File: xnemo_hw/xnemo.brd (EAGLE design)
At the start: 39.7 x 29 mm, 20 parts, among them J1 MICRO_USB_B_RECEPT, J2 DM3D_MICRO_SD, U1 LTC3559, U2 L3GD20, U3 STM32F405RG, U5 HMC5883L, U6 ADXL345, X1 TXC_7A_XTAL

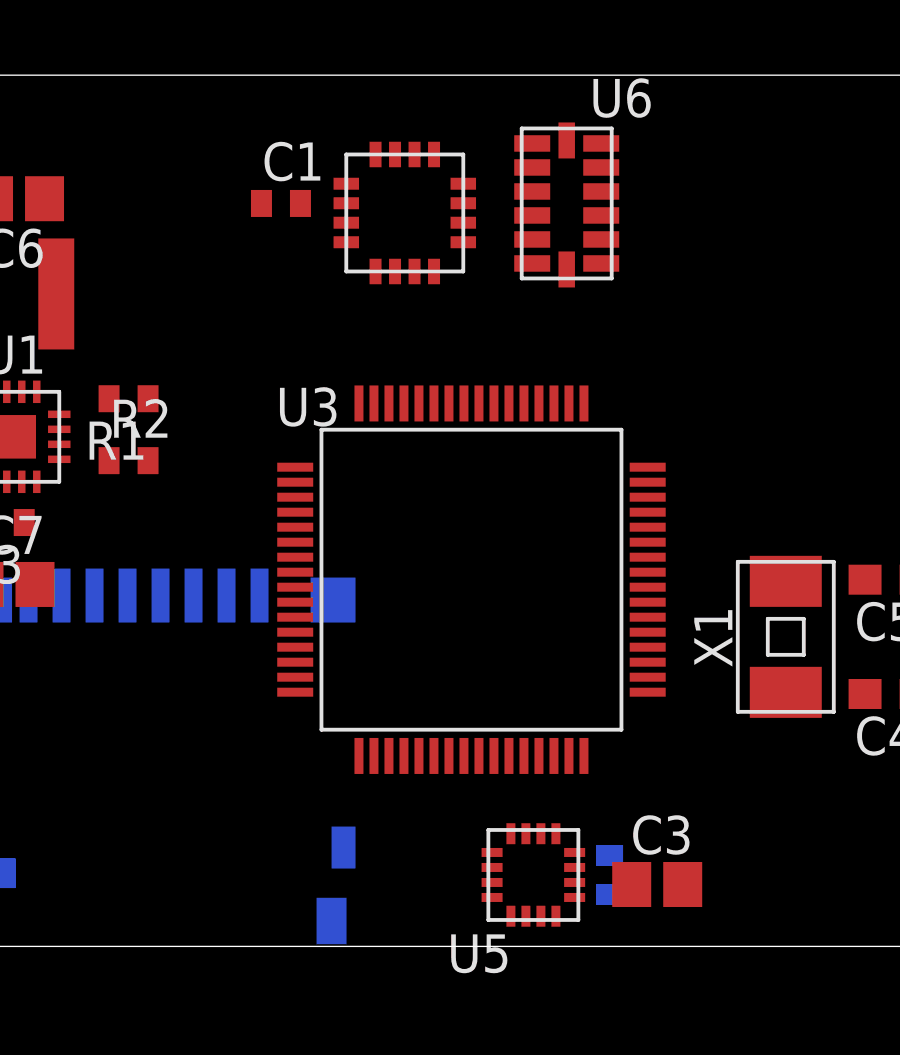
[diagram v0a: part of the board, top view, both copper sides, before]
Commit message: Updated some little things and added JTAG header
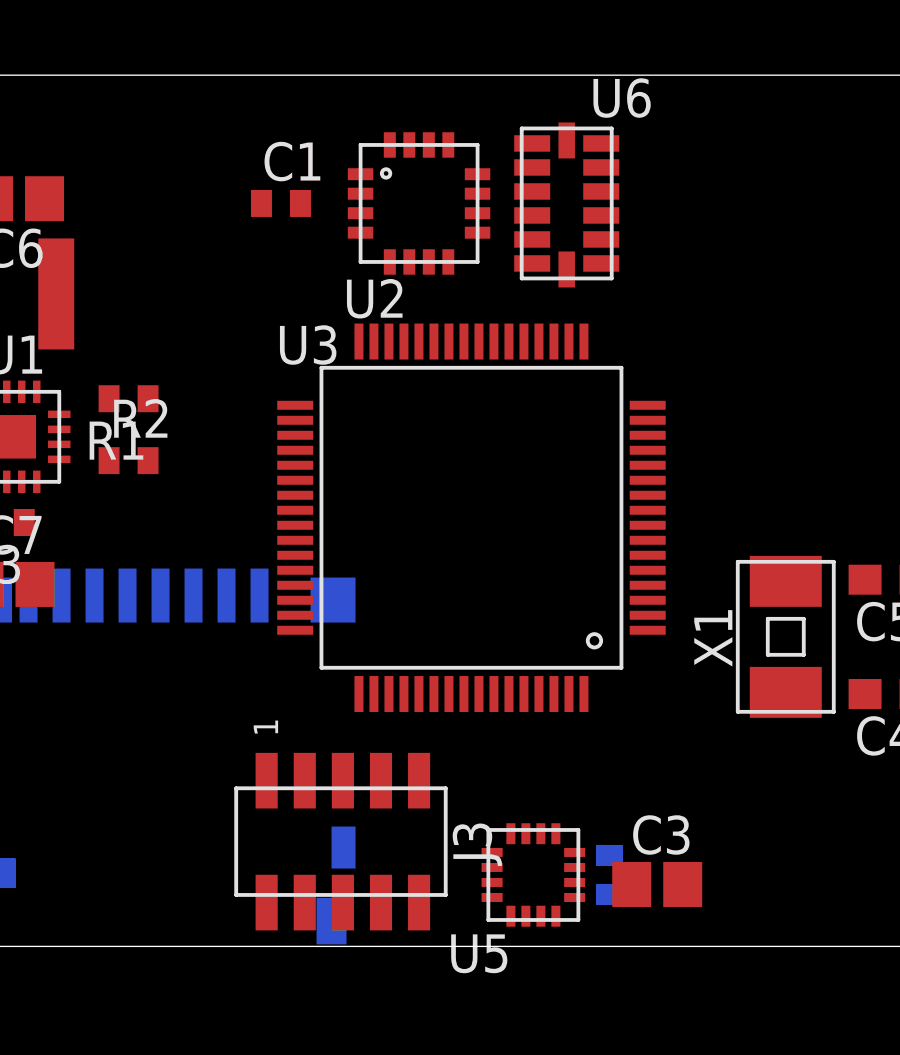
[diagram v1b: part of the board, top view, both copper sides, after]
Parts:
- added J3: HEADER_2X5, xnemo:HEADER_2X5_0.05_SMD
- moved U3 2.06 mm to (23.7, 14.3)
- moved U2 0.57 mm to (21.9, 24.8), turned to 0 degrees
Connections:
- net USB_HPWR renamed POW_HPWR
- net USB_SUSP renamed POW_SUSP
- new net JNTRST: U3.P$56
- new net JTCK: J3.4, U3.P$49
- new net JTDI: J3.8, U3.P$50
- new net JTDO: J3.6, U3.P$55
- new net JTMS: J3.2, U3.P$46
- new net POW_CHRG: U1.P$15
- new net RESET: J3.10, U3.P$7
- net 3V3: now also J3.1
- net GND: now also J3.3, J3.5, J3.7, J3.9

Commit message: Started bord
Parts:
- added C10, C11, C12, C9: 2.2u, resistor:C0603
- C4, C5: device resistor:C0603 -> resistor:C0402
- moved J3 10.5 mm to (8.89, 3.49)
- moved U2 8.04 mm to (14.0, 23.5), turned to 180 degrees
- moved U5 6.35 mm to (19.4, 2.54)
- moved C3 5.41 mm to (24.4, 2.38)
- moved U6 5.08 mm to (21.7, 24.9), turned to 270 degrees
- moved C4 4.98 mm to (32.7, 9.21), turned to 270 degrees
- moved C5 4.92 mm to (32.7, 12.4), turned to 90 degrees
- moved X1 4.00 mm to (30.2, 10.8)
- moved C1 3.74 mm to (13.7, 24.0), flipped to the bottom, turned to 270 degrees
- moved U3 3.17 mm to (21.1, 12.4)
- moved U1 2.43 mm to (6.03, 17.5)
- moved C2 2.23 mm to (26.0, 2.54)
- moved R2 2.01 mm to (10.3, 16.8), turned to 180 degrees
- moved R1 1.91 mm to (10.3, 18.3), turned to 0 degrees
- moved C8 0.79 mm to (4.13, 20.6), turned to 0 degrees
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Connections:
- net N$5 renamed GYR_RES
- removed net VBUS: C7.2, U1.P$16
- new net N$17: C10.1, U3.P$31
- new net N$5: C11.1, U3.P$47
- net 3V3: now also C12.1, C9.2
- net ACC_INT1: now also U3.P$27
- net ACC_INT2: now also U3.P$26
- net GND: now also C10.2, C11.2, C12.2, C9.1
- net GYR_DRDY: now also U3.P$34
- net GYR_INT1: now also U3.P$33
- net POW_CHRG: now also U3.P$28
- net POW_HPWR: now also U3.P$30
- net POW_SUSP: now also U3.P$29
- net SPI_CS_ACC: now also U3.P$25
- net SPI_CS_GYR: now also U3.P$35
- net VUSB: now also C7.2, U1.P$16
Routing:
- net 3V3: track 0.00 -> 30.6 mm
- net RESET: track 0.00 -> 23.5 mm, vias 0 -> 2
- net GYR_DRDY: track 0.00 -> 18.9 mm, vias 0 -> 2
- net SPI_CLK: track 0.00 -> 18.7 mm, vias 0 -> 2
- net GYR_INT1: track 0.00 -> 14.7 mm, vias 0 -> 2
- net JTDO: track 0.00 -> 14.6 mm
- net JTMS: track 0.00 -> 14.6 mm
- net JTCK: track 0.00 -> 12.5 mm
- net USB_D-: track 0.00 -> 11.0 mm
- net USB_D+: track 0.00 -> 11.0 mm
- net JTDI: track 0.00 -> 10.7 mm, vias 0 -> 2
- net SD_DAT3: track 0.00 -> 10.2 mm, vias 0 -> 1
- net SPI_MISO: track 0.00 -> 8.53 mm, vias 0 -> 1
- net SPI_MOSI: track 0.00 -> 8.01 mm, vias 0 -> 2
- net OSC_IN: track 0.00 -> 6.57 mm
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- added copper zone on layer 1, net GND
- added copper zone on layer 16, net GND

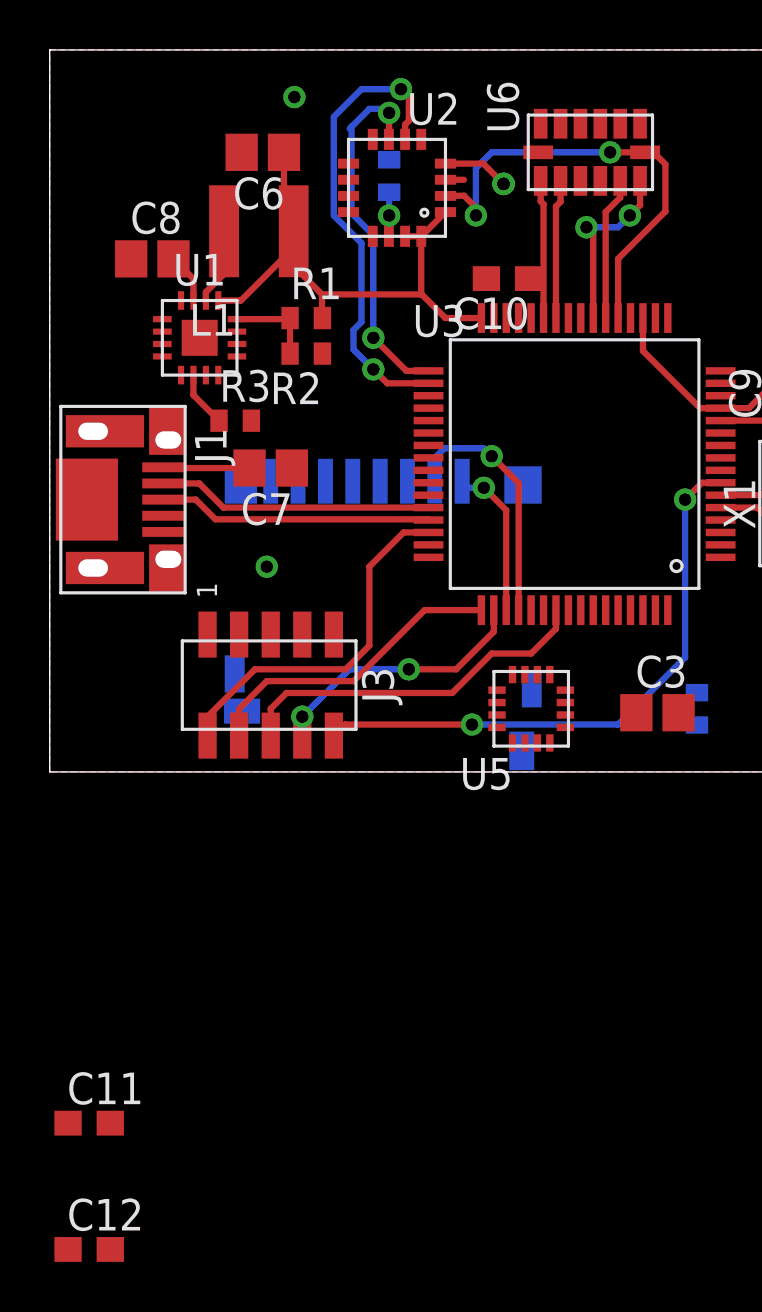
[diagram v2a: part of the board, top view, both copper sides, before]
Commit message: Most of the PCB is routed
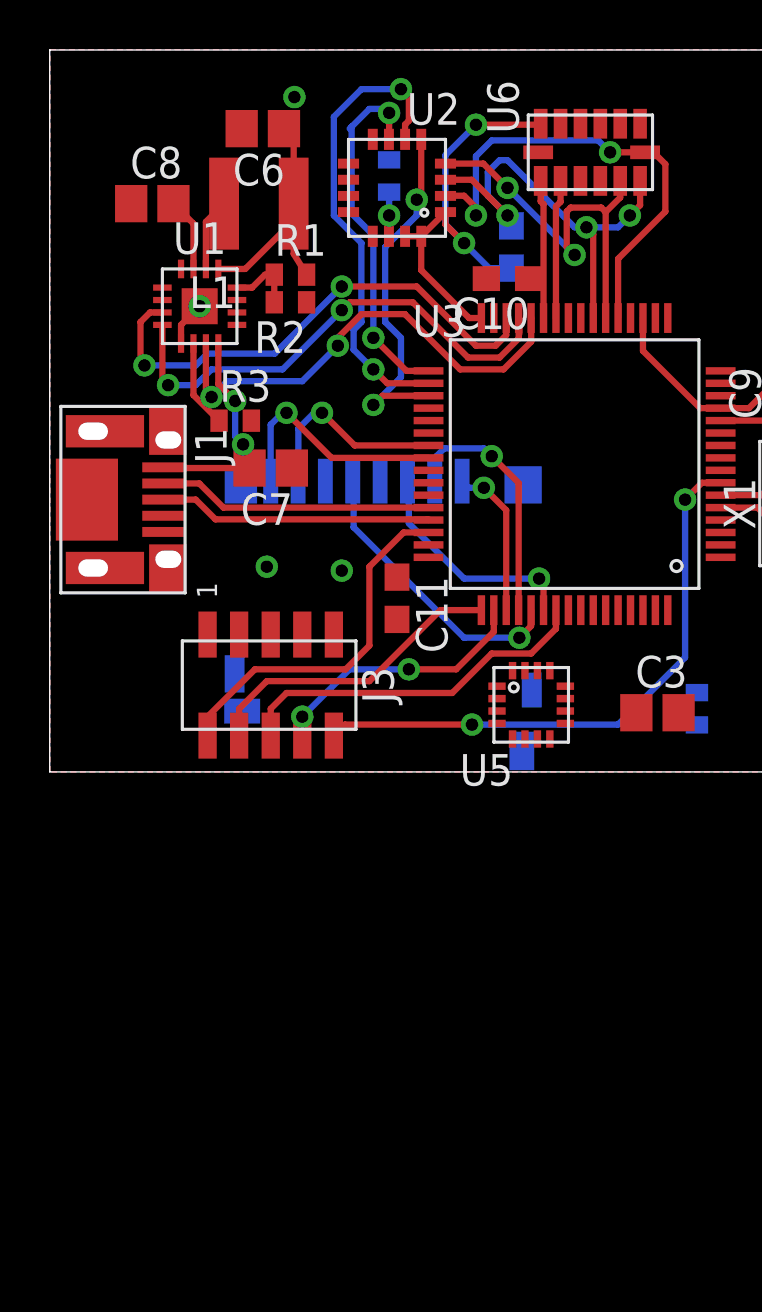
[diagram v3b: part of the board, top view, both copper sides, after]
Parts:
- moved C12 43.8 mm to (18.6, 21.1), flipped to the bottom, turned to 90 degrees
- moved C11 24.5 mm to (14.0, 6.99), turned to 270 degrees
- moved C8 2.22 mm to (4.13, 22.9)
- moved R2 2.16 mm to (9.68, 18.9)
- moved R1 1.86 mm to (9.68, 20.0)
- moved U1 1.27 mm to (6.03, 18.7)
- moved L1 1.11 mm to (8.41, 22.9)
- moved C6 0.95 mm to (8.57, 25.9)
- moved U5 0.16 mm to (19.4, 2.70)
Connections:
- net N$17 renamed VCAP_1
- net N$5 renamed VCAP_2
- net POW_HPWR: now also U3.P$29; no longer U3.P$30
- net POW_SUSP: now also U3.P$30; no longer U3.P$29
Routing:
- net POW_HPWR: track 0.00 -> 20.7 mm, vias 0 -> 2
- net POW_SUSP: track 0.00 -> 20.6 mm, vias 0 -> 2
- net POW_CHRG: track 0.00 -> 19.0 mm, vias 0 -> 2
- net SPI_CS_GYR: track 0.00 -> 14.4 mm, vias 0 -> 2
- net SD_CLK: track 0.00 -> 11.7 mm, vias 0 -> 1
- net SPI_MOSI: track 8.01 -> 17.7 mm, vias 2 -> 3
- net SD_DAT1: track 0.00 -> 9.57 mm, vias 0 -> 1
- net SD_CMD: track 0.00 -> 9.22 mm, vias 0 -> 1
- net SD_DAT0: track 0.00 -> 8.17 mm, vias 0 -> 1
- net SPI_MISO: track 8.53 -> 16.2 mm, vias 1 -> 2
- net 3V3: track 30.6 -> 37.7 mm, vias 0 -> 2
- net VUSB: track 3.46 -> 8.99 mm, vias 0 -> 2
- net GND: track 2.42 -> 4.23 mm, vias 2 -> 4
- net N$1: track 2.26 -> 3.53 mm
- net VBAT: track 2.01 -> 2.96 mm
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
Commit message: Mostly routed!
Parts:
- added C13: 100n, resistor:C0402
- added J4, J5: HEADER_2X5, xnemo:HEADER_2X5_0.05_SMD
- added R5, R6: 22k, resistor:R0402
- moved C12 8.73 mm to (26.4, 25.1), flipped to the top, turned to 270 degrees
- moved C7 4.47 mm to (4.60, 11.0), flipped to the bottom, turned to 90 degrees
- moved U5 3.58 mm to (22.9, 3.49)
- moved C3 3.43 mm to (27.8, 3.17), turned to 270 degrees
- moved R3 3.02 mm to (4.45, 14.1), flipped to the bottom
- moved L1 2.16 mm to (6.67, 24.1)
- moved C6 2.03 mm to (6.99, 27.1)
- moved C8 2.02 mm to (2.70, 24.3), turned to 270 degrees
- moved U1 1.81 mm to (4.60, 19.8)
- moved R1 1.69 mm to (8.57, 21.3)
- moved R2 1.57 mm to (8.57, 20.0)
- moved C2 1.43 mm to (26.0, 3.97), flipped to the top
- moved C9 0.79 mm to (30.2, 15.1), turned to 180 degrees
- moved C11 0.32 mm to (14.0, 6.67)
- moved C10 0.32 mm to (18.1, 19.8), turned to 0 degrees
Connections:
- net N$1 renamed POW_PROG
- removed net JNTRST: U3.P$56
- new net N$1: J5.4
- new net N$15: J4.10
- new net N$16: J5.7
- new net N$17: J5.5
- new net N$2: J5.2
- new net N$3: J5.3
- new net N$4: J5.1
- new net N$5: J5.6
- new net N$6: J5.8
- new net N$7: J4.9
- new net N$8: J5.10
- new net N$9: J5.9
- new net PA0: J4.6, U3.P$14
- new net PA1: J4.5, U3.P$15
- new net PA2: J4.2, U3.P$16
- new net PA3: J4.1, U3.P$17
- new net PA4: J4.8, U3.P$20
- new net PC0: U3.P$8
- new net PC1: U3.P$9
- new net PC2: U3.P$10
- new net PC3: U3.P$11
- new net PC4: J4.7, U3.P$24
- net 3V3: now also C13.1, J4.4, R5.2, R6.2
- net GND: now also C13.2, J4.3, U1.P$9, U3.P$60
- net I2C_SCL: now also R6.1
- net I2C_SDA: now also R5.1
- net MAG_DRDY: now also U3.P$61
- net SD_DET: now also U3.P$56
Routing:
- net 3V3: track 37.7 -> 131.2 mm, vias 2 -> 8
- net SPI_CS_ACC: track 0.00 -> 27.3 mm, vias 0 -> 2
- net PC4: track 0.00 -> 17.4 mm, vias 0 -> 2
- net SD_DET: track 0.00 -> 16.7 mm, vias 0 -> 1
- net PA4: track 0.00 -> 14.5 mm, vias 0 -> 2
- net VUSB: track 8.99 -> 21.1 mm, vias 2 -> 1
- net PA1: track 0.00 -> 11.8 mm
- net GND: track 4.23 -> 15.5 mm, vias 4 -> 30
- net VBAT: track 2.96 -> 13.0 mm, vias 0 -> 2
- net PA3: track 0.00 -> 9.04 mm
- net PA0: track 0.00 -> 8.44 mm
- net I2C_SCL: track 0.00 -> 5.76 mm, vias 0 -> 1
- net PA2: track 0.00 -> 5.39 mm, vias 0 -> 2
- net I2C_SDA: track 0.00 -> 5.10 mm, vias 0 -> 1
- net MAG_C1: track 0.00 -> 3.85 mm
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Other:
- board size 39.7 x 29 mm -> 39.7 x 29.8 mm

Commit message: Passes DRC
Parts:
- added C14: 22p, resistor:C0402
- C7: value 10u -> 1u; device resistor:C0805 -> resistor:C0603
- moved C6 0.95 mm to (6.99, 28.1)
- moved L1 0.79 mm to (6.67, 24.9)
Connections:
- removed net N$15: J4.10
- net 3V3: now also C14.2
- net BUCK_FB1: now also C14.1
- net GND: now also U5.P$11
- net PA0: now also J4.8; no longer J4.6
- net PA1: now also J4.6
- net PA4: now also J4.10; no longer J4.8
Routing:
- net GND: track 15.5 -> 21.4 mm, vias 30 -> 34
- net PA1: track 11.8 -> 7.77 mm
- net 3V3: track 131.2 -> 134.7 mm, vias 8 -> 9
- net BUCK_FB1: track 3.02 -> 5.58 mm, vias 0 -> 1
- net MAG_SETP: track 2.92 -> 5.17 mm
- net PA4: track 14.5 -> 15.6 mm
- net PA0: track 8.44 -> 9.43 mm
- net BUCK_SW1: track 2.96 -> 3.65 mm

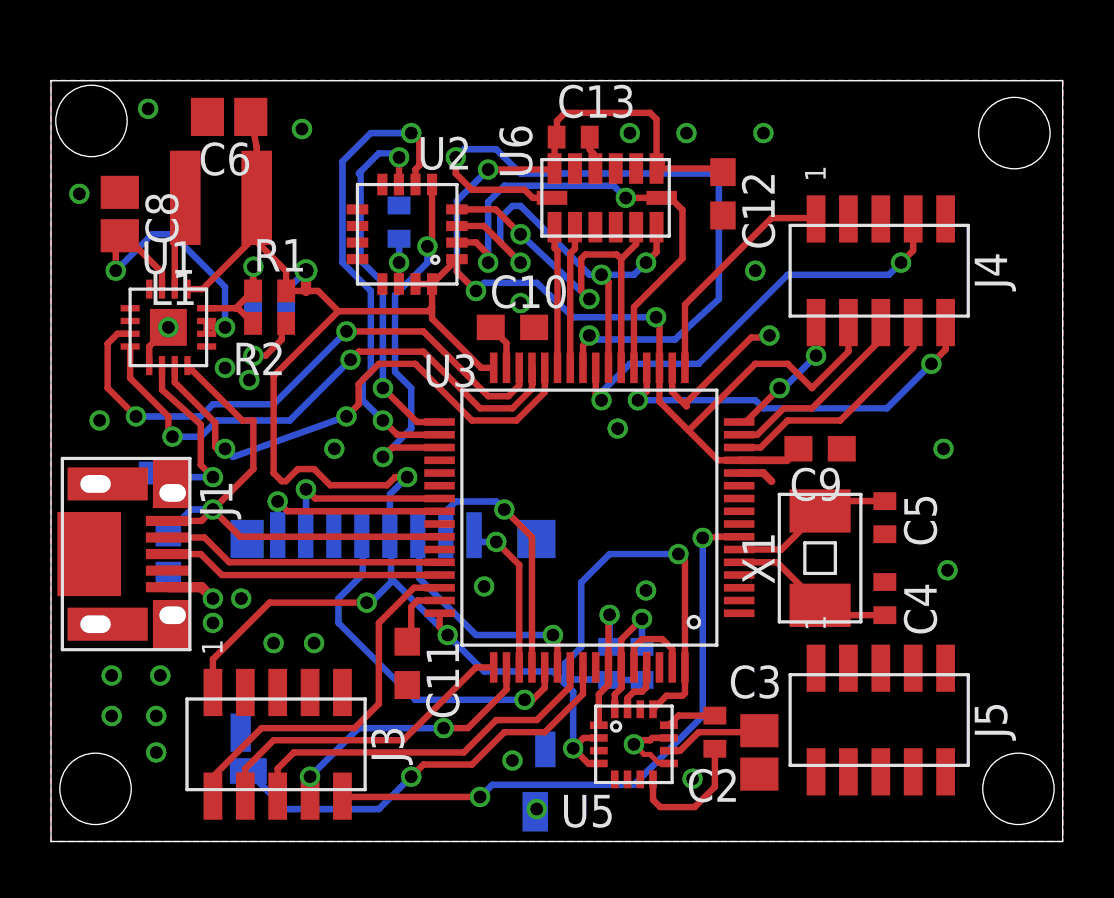
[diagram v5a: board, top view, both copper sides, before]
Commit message: Expansion headers are now thru-hole
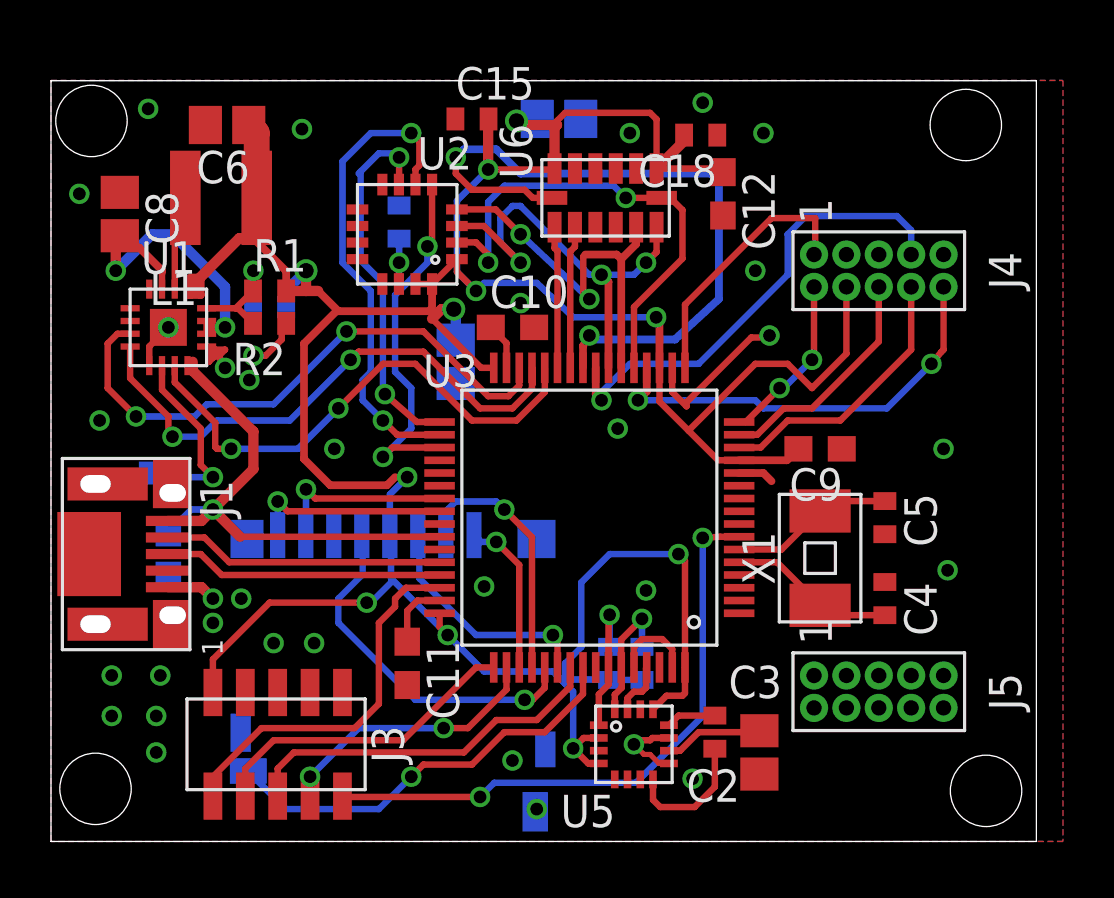
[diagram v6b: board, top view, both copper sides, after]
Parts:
- removed C13: 100n, resistor:C0402
- added C15: 220n, resistor:C0402
- added C16, C17: 10u, resistor:C0805
- added C18: 100n, resistor:C0402
- C1: value (none) -> 10n
- C8: value 2.2u -> 4.7u
- J3: value HEADER_2X5 -> HEADER_2X5_0.05_SMD
- J4, J5: value HEADER_2X5 -> HEADER_2X5_0.05_THRU; device xnemo:HEADER_2X5_0.05_SMD -> xnemo:HEADER_2X5_0.05_THRU
- R3: value (none) -> 1.74k
- moved J5 1.11 mm to (32.5, 5.56)
- moved C6 0.33 mm to (6.91, 27.8)
- moved J4 0.08 mm to (32.5, 22.1)
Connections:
- net 3V3: now also C15.2, C16.1, C17.1, C18.2, J4.P$4; no longer C13.1, J4.4
- net GND: now also C15.1, C16.2, C17.2, C18.1, J4.P$3; no longer C13.2, J4.3
- net N$1: now also J5.P$4; no longer J5.4
- net N$16: now also J5.P$7; no longer J5.7
- net N$17: now also J5.P$5; no longer J5.5
- net N$2: now also J5.P$2; no longer J5.2
- net N$3: now also J5.P$3; no longer J5.3
- net N$4: now also J5.P$1; no longer J5.1
- net N$5: now also J5.P$6; no longer J5.6
- net N$6: now also J5.P$8; no longer J5.8
- net N$7: now also J4.P$9; no longer J4.9
- net N$8: now also J5.P$10; no longer J5.10
- net N$9: now also J5.P$9; no longer J5.9
- net PA0: now also J4.P$8; no longer J4.8
- net PA1: now also J4.P$5, J4.P$6; no longer J4.5, J4.6
- net PA2: now also J4.P$2; no longer J4.2
- net PA3: now also J4.P$1; no longer J4.1
- net PA4: now also J4.P$10; no longer J4.10
- net PC4: now also J4.P$7; no longer J4.7
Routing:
- net 3V3: track 134.7 -> 144.7 mm, vias 9 -> 11
- net GND: track 21.4 -> 22.9 mm
- net PA3: track 9.04 -> 10.4 mm
- net PA2: track 5.39 -> 6.76 mm
- net PA0: track 9.43 -> 10.8 mm
- net PA1: track 7.77 -> 9.13 mm
- net PC4: track 17.4 -> 18.8 mm, vias 2 -> 1
- net PA4: track 15.6 -> 17.0 mm
- net VBAT: track 13.0 -> 13.6 mm
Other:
- board size 39.7 x 29.8 mm -> 38.6 x 29.8 mm
